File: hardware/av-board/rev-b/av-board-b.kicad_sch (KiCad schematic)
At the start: 163 parts, among them J1 RCA Y, J10 2x20 socket, J2 RCA Pb, J3 RCA Pr, J4 RCA L, J5 RCA R, J6 HDMI-001, J9 2x20 socket, SW1 TS-1187A-B-A-B, SW2 TS-1187A-B-A-B, U1 ADV7181DBCPZ-RL, U10 TPD4E05U06DQAR, U11 TPD4E05U06DQAR, U2 ADV7511KSTZ, U3 PCM1808PWR, U4 TLV62569DBVR, U5 TPS7A7001DDAR, U6 TPS7A7001DDAR, U7 TPS7A7001DDAR, U8 TPD4E05U06DQAR, U9 TPD4E05U06DQAR, Y1 28.63636MHz 20pF

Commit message: AV boards: second full review, ESD at the connectors, rev C, rev B and C-B routed
Rev C (the SOM on its own carrier, C-A with the ADV7511, C-B with the SN65DP159) joins rev B on
shared code: kit/circuits.py (rev B's circuits), kit/adv7181d_layout.py, kit/tmds_layout.py,
rev-c/ (carrier, floor plan, SOM pin matching, design notes, review).

Review fixes (rev-b/review.md, rev-c/review.md):
- ESD at each connector: a TPD1E05U06 per video and S/PDIF input (the shared four-line arrays
  sat 11-25 mm from some of their connectors); every ESD part placed first, at its connector;
  an array's ground through the package to one via away from the connector (TI's layout); the
  VGA array's channels in the header's order; rev C's USB-C TVS between receptacle and fuse.
- XIAO: an ESP32-C3 boots right (SCK pulled up for GPIO8, TMS on D0 for GPIO2, 470 R on the
  translator's outputs for GPIO9's BOOT button).
- Rev B: J10 pins 29/30 (the Console's SDRAM EXIO pins, which a MiSTer-style fit puts on 3.3 V
  and GND) left open.
- D6 drawn as the unidirectional TVS it is.

Kit: plane vias never in pads, by true circle-to-box distance; analog lines and references kept
0.5 mm from digital ones by the router (Freerouting class-to-class rules); rip-up in the
finisher, kept only when it leaves fewer gaps; xtalk.py counts each close run once.

Rev B and C-B: routed, DRC clean, no unconnected items; schematics, fab files and renders
regenerated. C-A's routed board follows.

Co-Authored-By: Claude Opus 5.5 <noreply@anthropic.com>
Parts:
- removed FB5: 120R, Inductor_SMD:L_0603_1608Metric, symbol Device:FerriteBead
- removed U11: TPD4E05U06DQAR, lcsc:USON-10_L2.5-W1.0-P0.50-BL, symbol lcsc:TPD4E05U06DQAR_C138714
- added C77, C81, C82, C83, C84, C85, C86, C87, C88, C89, C90, C91, C92: 100n, Capacitor_SMD:C_0402_1005Metric, symbol Device:C
- added C78, C79, C80: 10u, Capacitor_SMD:C_0603_1608Metric, symbol Device:C
- added D10, D11, D12, D13, D8, D9: TPD1E05U06DPYR, lcsc:X1SON-2_L1.0-W0.6-P0.65-RD-1, symbol lcsc:TPD1E05U06DPYR
- added D2: KT-0603R, lcsc:LED-SMD_L1.6-W0.8-R-RD, symbol lcsc:KT-0603R
- added D3: B5819W, Diode_SMD:D_SOD-123, symbol Device:D_Schottky
- added D7: 1N4148WS, Diode_SMD:D_SOD-323, symbol Device:D
- added F2: 0.2A, lcsc:F0805, symbol lcsc:BSMD0805-020-30V
- added J11: XIAO 5V..D7, lcsc:HDR-TH_7P-P2.54-V-F, symbol lcsc:HXPM2.54-1X7PZC-Y
- added J12: XIAO D0..D6, lcsc:HDR-TH_7P-P2.54-V-F, symbol lcsc:HXPM2.54-1X7PZC-Y
- added J13: SPDIF, lcsc:HDR-TH_5P-P2.54-V-M, symbol lcsc:PZ254V-11-05P
- added J7: SYNC, lcsc:HDR-TH_2P-P2.54-V-M, symbol lcsc:PZ254V-11-02P
- added J8: VGA, lcsc:HDR-TH_16P-P2.54-V-M-R2-C8-S2.54, symbol lcsc:Header-Male-2.54_2x8
- added Q1, Q2: 2N7002, lcsc:SOT-23-3_L2.9-W1.3-P1.90-LS2.4-BR, symbol lcsc:2N7002
- added R52: 47k, Resistor_SMD:R_0402_1005Metric, symbol Device:R
- added R53, R54, R55, R57, R59, R77: 10k, Resistor_SMD:R_0402_1005Metric, symbol Device:R
- added R56, R58: 12k, Resistor_SMD:R_0402_1005Metric, symbol Device:R
- added R60: 75, Resistor_SMD:R_0603_1608Metric, symbol Device:R
- added R61: 1M, Resistor_SMD:R_0402_1005Metric, symbol Device:R
- added R62, R64: 33, Resistor_SMD:R_0402_1005Metric, symbol Device:R
- added R63: 100k, Resistor_SMD:R_0402_1005Metric, symbol Device:R
- added R65, R66, R67, R68, R69: 49.9, Resistor_SMD:R_0402_1005Metric, symbol Device:R
- added R70: 887, Resistor_SMD:R_0402_1005Metric, symbol Device:R
- added R71, R72, R73, R74, R75, R76: 2k, Resistor_SMD:R_0402_1005Metric, symbol Device:R
- added R78: 27k, Resistor_SMD:R_0402_1005Metric, symbol Device:R
- added U12: TPS7A2045PDBVR, lcsc:SOT-23-5_L2.9-W1.6-P0.95-LS2.8-BR, symbol lcsc:TPS7A2045PDBVR
- added U13: SN74LVC1GU04DBVR, lcsc:SOT-23-5_L3.0-W1.7-P0.95-LS2.8-BR, symbol lcsc:SN74LVC1GU04DBVR
- added U14, U15: SN74LVC1G04DBVR, lcsc:SOT-23-5_L3.0-W1.7-P0.95-LS2.8-BR, symbol lcsc:SN74LVC1G04DBVR
- added U19, U20: TPD4E05U06DQAR, lcsc:USON-10_L2.5-W1.0-P0.50-BL, symbol lcsc:TPD4E05U06DQAR_C138714
- added U21: SN74LVC2G17DBVR, lcsc:SOT-23-6_L2.9-W1.6-P0.95-LS2.8-BL, symbol lcsc:SN74LVC2G17DBVR
- added U22: SN74LVC8T245PWR, lcsc:TSSOP-24_L7.8-W4.4-P0.65-LS6.4-BL, symbol lcsc:SN74LVC8T245PWR
- added U23: SN74AVC4T245PWR, lcsc:TSSOP-16_L5.0-W4.4-P0.65-LS6.4-BL, symbol lcsc:SN74AVC4T245PWR
- C11: value 10u -> 6.8p; footprint Capacitor_SMD:C_0805_2012Metric -> Capacitor_SMD:C_0402_1005Metric; LCSC C15850 -> C1576
- C12, C15, C9: value 220p -> 10u; footprint Capacitor_SMD:C_0402_1005Metric -> Capacitor_SMD:C_0805_2012Metric; LCSC C1530 -> C15850
- C14: value 10u -> 220p; footprint Capacitor_SMD:C_0805_2012Metric -> Capacitor_SMD:C_0402_1005Metric; LCSC C15850 -> C1530
- C16, C18, C19: footprint Capacitor_SMD:C_0603_1608Metric -> Capacitor_SMD:C_0805_2012Metric; LCSC C19702 -> C15850
- C17, C20: value 10u -> 220p; footprint Capacitor_SMD:C_0603_1608Metric -> Capacitor_SMD:C_0402_1005Metric; LCSC C19702 -> C1530
- C23, C24, C66, C68: value 100n -> 10u; footprint Capacitor_SMD:C_0402_1005Metric -> Capacitor_SMD:C_0603_1608Metric; LCSC C1525 -> C19702
- C26: value 1n -> 100n; LCSC C1523 -> C1525
- C27: value 33p -> 100n; LCSC C1562 -> C1525
- C28: value 33p -> 1n; LCSC C1562 -> C1523
- C29: value 100n -> 1n; LCSC C1525 -> C1523
- C30: value 100n -> 33p; LCSC C1525 -> C1562
- C31: value 10u -> 33p; footprint Capacitor_SMD:C_0603_1608Metric -> Capacitor_SMD:C_0402_1005Metric; LCSC C19702 -> C1562
- C33, C46, C48, C50, C52, C54: value 10n -> 100n; LCSC C15195 -> C1525
- C34, C37: footprint Capacitor_SMD:C_0603_1608Metric -> Capacitor_SMD:C_0402_1005Metric; LCSC C19702 -> C15525
- C39: value 10u -> 10n; footprint Capacitor_SMD:C_0603_1608Metric -> Capacitor_SMD:C_0402_1005Metric; LCSC C19702 -> C15195
- C40: value 100n -> 10u; LCSC C1525 -> C15525
- C41: value 82n -> 100n; LCSC C277511 -> C1525
- C42: value 10n -> 10u; LCSC C15195 -> C15525
- C44: value 10n -> 82n; LCSC C15195 -> C277511
- C45, C51, C53, C55, C57, C59: value 100n -> 10n; LCSC C1525 -> C15195
- C5, C7, C8: value 10u -> 100n; footprint Capacitor_SMD:C_0805_2012Metric -> Capacitor_SMD:C_0402_1005Metric; LCSC C15850 -> C1525
- C56, C58, C60: value 10u -> 100n; footprint Capacitor_SMD:C_0603_1608Metric -> Capacitor_SMD:C_0402_1005Metric; LCSC C19702 -> C1525
- C6: value 6.8p -> 100n; LCSC C1576 -> C1525
- C61: value 220p -> 10n; LCSC C1530 -> C15195
- C63: value 220p -> 100n; LCSC C1530 -> C1525
- C64: value 1u -> 10u; LCSC C15849 -> C19702
- C69, C71: value 100n -> 220p; LCSC C1525 -> C1530
- C70, C72: value 100n -> 1u; footprint Capacitor_SMD:C_0402_1005Metric -> Capacitor_SMD:C_0603_1608Metric; LCSC C1525 -> C15849
- R10, R8: value 30.1k -> 10k; LCSC C29402 -> C25744
- R11, R12: value 75 -> 10k; footprint Resistor_SMD:R_0603_1608Metric -> Resistor_SMD:R_0402_1005Metric; LCSC C4275 -> C25744
- R13: value 75 -> 499k; footprint Resistor_SMD:R_0603_1608Metric -> Resistor_SMD:R_0402_1005Metric; LCSC C4275 -> C25793
- R14: value 1M -> 100k; LCSC C26083 -> C25741
- R15: value 1.69k -> 169k; LCSC C25870 -> C25758
- R16, R18, R20: value 33 -> 30.1k; LCSC C25105 -> C29402
- R17, R19: value 33 -> 78.7k; LCSC C25105 -> C67239
- R21, R22, R23: value 33 -> 75; footprint Resistor_SMD:R_0402_1005Metric -> Resistor_SMD:R_0603_1608Metric; LCSC C25105 -> C4275
- R24: value 4.7k -> 75; footprint Resistor_SMD:R_0402_1005Metric -> Resistor_SMD:R_0603_1608Metric; LCSC C25900 -> C4275
- R25: value 4.7k -> 1M; LCSC C25900 -> C26083
- R26: value 4.7k -> 1.69k; LCSC C25900 -> C25870; Note held in reset until the FPGA drives it (5 ms low minimum [D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 -> (none)
- R27, R28, R29: value 4.7k -> 33; LCSC C25900 -> C25105
- R3: value 499k -> 470; LCSC C25793 -> C25117
- R30, R31, R32, R33, R34: value 10k -> 33; LCSC C25744 -> C25105
- R35, R36, R38, R39: value 10k -> 4.7k; LCSC C25744 -> C25900
- R37: value 10k -> 4.7k; LCSC C25744 -> C25900; Note (none) -> held in reset until the FPGA drives it (5 ms low minimum [D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
- R40: value 49.9 -> 4.7k; LCSC C25120 -> C25900
- R41: value 49.9 -> 10k; LCSC C25120 -> C25744
- R42, R43: value 49.9 -> 75; footprint Resistor_SMD:R_0402_1005Metric -> Resistor_SMD:R_0603_1608Metric; LCSC C25120 -> C4275
- R44: value 887 -> 75; footprint Resistor_SMD:R_0402_1005Metric -> Resistor_SMD:R_0603_1608Metric; LCSC C55968414 -> C4275
- R45, R46: value 2k -> 10k; LCSC C4109 -> C25744
- R47, R48: value 2k -> 33; LCSC C4109 -> C25105
- R49: value 2k -> 4.7k; LCSC C4109 -> C25900
- R5: value 169k -> 470; LCSC C25758 -> C25117
- R50: value 2k -> 47k; LCSC C4109 -> C25792
- R51: value 10k -> 4.7k; LCSC C25744 -> C25900; Note 0 V on HPD with no sink [HWG 6.1.4: 10 k +-10 %] -> (none)
- R6: value 30.1k -> 470; LCSC C29402 -> C25117
- R7, R9: value 78.7k -> 10k; LCSC C67239 -> C25744
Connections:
- net +5V: now also C62.1, C9.1, D3.2 (A), F2.1, U12.1 (IN), U12.3 (EN); no longer C4.1
- net 1V8A: now also C16.1, C17.1, R17.1; no longer C11.1, C12.1, R7.1
- net 1V8B: now also C19.1, C20.1, R19.1; no longer C14.1, C15.1, R9.1
- net 3V3: now also C14.1, C15.1, C18.1, C49.1, C6.1, C67.1, C68.1, C76.1, R10.2, R11.2, R12.2, R15.1, R35.1, R36.1, R49.1, R51.1, C77.1, C91.1, Q1.1 (G), Q2.1 (G), R71.1, R72.1, R73.1, R78.1, U13.5 (VCC), U14.5 (VCC), U15.5 (VCC), U21.5 (VCC), U22.23 (VCCB), U22.24 (VCCB), U23.16 (VCCB); no longer C10.1, C59.1, C60.1, C9.1, R24.1, R25.1, R45.1, R46.1, R47.1, R5.1
- net 3V6: now also C10.1, C11.1, C12.1, R13.1; no longer C5.1, C6.1, C7.1, R3.1
- net 5VA: now also C65.1, C66.1, U12.5 (OUT); no longer C57.1, C58.1
- net AIN_PB: now also C26.2; no longer C24.2
- net AIN_PR: now also C27.2; no longer C25.2
- net AIN_Y: now also C25.2; no longer C23.2
- net ALSB: now also R39.2; no longer R28.2
- net AUD_DIV_L: now also C69.1, C70.1, R56.2, R57.1; no longer C61.1, C62.1, R36.2, R37.1
- net AUD_DIV_R: now also C71.1, C72.1, R58.2, R59.1; no longer C63.1, C64.1, R38.2, R39.1
- net AUD_VINL: now also C70.2; no longer C62.2
- net AUD_VINR: now also C72.2; no longer C64.2
- net AV_AVDD: now also C23.1, C60.1, C61.1; no longer C18.1, C53.1, C54.1
- net AV_C0: now also R31.1; no longer R20.1
- net AV_C1: now also R30.1; no longer R19.1
- net AV_C5: now also R29.1; no longer R18.1
- net AV_C6: now also R28.1; no longer R17.1
- net AV_C7: now also R27.1; no longer R16.1
- net AV_DE: now also R34.1; no longer R23.1
- net AV_DVDD: now also C21.1, C54.1, C55.1, C56.1, C57.1; no longer C16.1, C47.1, C48.1, C49.1, C50.1
- net AV_DVDDIO: now also C24.1, C50.1, C51.1, C52.1, C53.1, R38.1, R39.1, R40.1; no longer C19.1, C43.1, C44.1, C45.1, C46.1, R27.1, R28.1, R29.1
- net AV_HS: now also R32.1; no longer R21.1
- net AV_PVDD: now also C22.1, C44.2, C45.2, C58.1, C59.1; no longer C17.1, C41.2, C42.2, C51.1, C52.1
- net AV_VS: now also R33.1; no longer R22.1
- net CAPC2: now also C37.1, C38.1, C39.1; no longer C34.1, C35.1, C36.1
- net CAPY1: now also C34.1, C35.1, C36.1; no longer C31.1, C32.1, C33.1
- net CAPY2: now also C32.1, C33.1, C37.2, C38.2, C39.2; no longer C29.1, C30.1, C31.2, C32.2, C33.2
- net CML: now also C42.1, C43.1; no longer C39.1, C40.1
- net ELPF: now also C45.1, R26.1; no longer C42.1, R15.1
- net ELPF_RC: now also C44.1, R26.2; no longer C41.1, R15.2
- net FB_1V8A: now also C17.2, R17.2, R18.1; no longer C12.2, R7.2, R8.1
- net FB_1V8B: now also C20.2, R19.2, R20.1; no longer C15.2, R10.1, R9.2
- net FB_3V3: now also C14.2, R15.2, R16.1; no longer C9.2, R5.2, R6.1
- net FB_3V6: now also C11.2, R13.2, R14.1; no longer C6.2, R3.2, R4.1
- net FMT: now also R55.1; no longer R35.1
- net GND: now also C12.2, C15.2, C23.2, C24.2, C31.2, C32.2, C33.2, C41.2, C42.2, C6.2, C62.2, C64.2, C9.2, R14.2, R16.2, R18.2, R20.2, R21.2, R22.2, R23.2, R24.2, R41.2, R42.2, R43.2, R45.2, R46.2, R9.2, C77.2, C78.2, C79.2, C80.2, C81.2, C82.2, C83.2, C84.2, C85.2, C86.2, C87.2, C88.2, C89.2, C90.2, C91.2, C92.2, D10.2 (GND), D11.2 (GND), D12.2 (GND), D13.2 (GND), D2.2 (K), D8.2 (GND), D9.2 (GND), J11.2, J13.2, J13.4, J7.2, J8.10, J8.5, J8.6, J8.7, J8.8, R53.2, R54.2, R55.2, R57.2, R59.2, R60.2, R63.2, R70.2, R74.2, R77.2, U12.2 (GND), U13.3 (GND), U14.3 (GND), U15.3 (GND), U19.3 (GND), U19.8 (GND), U20.3 (GND), U20.8 (GND), U21.2 (GND), U22.10 (A8), U22.11 (GND), U22.12 (GND), U22.13 (GND), U22.22 (~{OE}), U22.6 (A4), U22.7 (A5), U22.8 (A6), U22.9 (A7), U23.10 (2B2), U23.11 (2B1), U23.14 (2#OE), U23.15 (1#OE), U23.2 (1DIR), U23.3 (2DIR), U23.8 (GND), U23.9 (GND); no longer C11.2, C14.2, C17.2, C20.2, C27.2, C28.2, C29.2, C37.2, C38.2, C39.2, C44.2, C45.2, C46.2, C47.2, C48.2, C70.2, C72.2, C74.2, J10.27, J10.28, J10.29, J10.30, J10.33, J10.34, J10.35, J10.36, J9.31, J9.32, J9.33, J9.34, J9.35, J9.36, R10.2, R11.2, R12.2, R13.2, R26.2, R30.2, R31.2, R32.2, R33.2, R34.2, R35.2, R39.2, R48.2, R51.2, R6.2, R8.2, U2.10 (SPDIF), U2.48 (CEC), U2.50 (CEC_CLK)
- net HDMI_5V: now also C92.1, F2.2, R75.1, R76.1; no longer C76.1, F1.2, R49.1, R50.1, U8.5 (D2-), U8.6 (NC)
- net HDMI_HPD: now also R77.1; no longer R51.1
- net HDMI_SCL: now also R75.2; no longer R49.2
- net HDMI_SDA: now also R76.2; no longer R50.2
- net IN_C0: now also R31.2; no longer R20.2
- net IN_C1: now also R30.2; no longer R19.2
- net IN_C5: now also R29.2; no longer R18.2
- net IN_C6: now also R28.2; no longer R17.2
- net IN_C7: now also R27.2; no longer R16.2
- net IN_DE: now also R34.2; no longer R23.2
- net IN_HS: now also R32.2; no longer R21.2
- net IN_INT: now also R38.2; no longer R27.2
- net IN_RESET_N: now also R37.1; no longer R26.1
- net IN_SCL: now also R35.2; no longer R24.2
- net IN_SDA: now also R36.2; no longer R25.2
- net IN_VS: now also R33.2; no longer R22.2
- net MD0: now also R53.1; no longer R33.1
- net MD1: now also R54.1; no longer R34.1
- net OUT_I2S0: now also R68.1; no longer R43.1
- net OUT_INT: now also R73.2; no longer R47.2
- net OUT_LRCLK: now also R67.1; no longer R42.1
- net OUT_MCLK: now also R65.1; no longer R40.1
- net OUT_PD: now also R74.1; no longer R48.1
- net OUT_SCL: now also R71.2; no longer R45.2
- net OUT_SCLK: now also R66.1; no longer R41.1
- net OUT_SDA: now also R72.2; no longer R46.2
- net PD_FB: now also R41.1; no longer R30.1
- net PWRDWN: now also R40.2; no longer R29.2
- net RCA_L: now also R56.1; no longer R36.1
- net RCA_PB: now also C26.1, R22.1, D9.1 (I/O); no longer C24.1, R12.1
- net RCA_PR: now also C27.1, R23.1, D10.1 (I/O); no longer C25.1, R13.1
- net RCA_R: now also R58.1; no longer R38.1
- net RCA_Y: now also C25.1, C28.1, R21.1, D8.1 (I/O); no longer C23.1, C26.1, R11.1
- net REFOUT: now also C40.1, C41.1; no longer C37.1, C38.1
- net R_EXT: now also R70.1; no longer R44.1
- net SYNC_Y: now also C28.2; no longer C26.2
- net TX_AVDD: now also C79.1, C85.1, C86.1, C87.1, C88.1; no longer C21.1, C69.1, C70.1, C71.1, C72.1
- net TX_DVDD: now also C78.1, C81.1, C82.1, C83.1, C84.1; no longer C20.1, C65.1, C66.1, C67.1, C68.1
- net TX_I2S0: now also R68.2; no longer R43.2
- net TX_LRCLK: now also R67.2; no longer R42.2
- net TX_MCLK: now also R65.2; no longer R40.2
- net TX_PLVDD: now also C80.1, C89.1, C90.1; no longer C22.1, C73.1, C74.1
- net TX_SCLK: now also R66.2; no longer R41.2
- net VREF: now also C63.1, C64.1; no longer C55.1, C56.1
- net XTAL: now also C30.1, R25.1; no longer C27.1, R14.1
- net XTAL1: now also C31.1, R25.2; no longer C28.1, R14.2
- net SYNC_G: now reaches U1.33 (SOG)
- net SYNC_G: now also C29.2
- net AIN_VG: now reaches U1.35 (AIN2)
- net AIN_VG: now also C47.2
- net AIN_VR: now reaches U1.46 (AIN7)
- net AIN_VR: now also C46.2
- net AIN_VB: now reaches U1.48 (AIN9)
- net AIN_VB: now also C48.2
- net HDMI_CEC: now reaches J6.13 (CEC)
- net HDMI_CEC: now also U2.48 (CEC), U8.5 (D2-), U8.6 (NC), D7.1 (K)
- net PD_HS_IN_CS_IN renamed VGA_HSIN
- net VGA_HSIN: now also R47.2; no longer R31.1
- net PD_VS_IN renamed VGA_VSIN
- net VGA_VSIN: now also R48.2; no longer R32.1
- new net CEC_PU: D7.2 (A), R78.2
- new net ESP_CS: J9.32, R10.1, U22.21 (B1)
- new net ESP_IRQ: J9.33, R11.1, U23.13 (1B1)
- new net ESP_MISO: J9.35, R12.1, U23.12 (1B2)
- new net ESP_MOSI: J9.36, U22.19 (B3)
- new net ESP_SCK: J9.34, U22.20 (B2)
- new net IN_LED: J10.33, R3.1
- new net LED_A: D2.1 (A), R3.2
- new net OUT_CECCLK: J9.31, U2.50 (CEC_CLK)
- new net OUT_SPDIF: J10.28, R69.1
- new net RCA_SYNC: C29.1, D11.1 (I/O), J7.1, R24.1
- new net SPDIF_5V: C73.1, F1.2, J13.5
- new net SPDIF_AC: C74.2, R61.2, U13.2 (A)
- new net SPDIF_AMP: R61.1, U13.4 (Y), U14.2 (A)
- new net SPDIF_COAX: C74.1, D12.1 (I/O), J13.1, R60.1
- new net SPDIF_OPT: D13.1 (I/O), J13.3, R63.1, U15.2 (A)
- new net SPDIF_ORX: J10.35, R64.2
- new net SPDIF_OSQ: R64.1, U15.4 (Y)
- new net SPDIF_RX: J10.27, R62.2
- new net SPDIF_SQ: R62.1, U14.4 (Y)
- new net TX_SPDIF: R69.2, U2.10 (SPDIF)
- new net VGA_5V: J8.9, R50.1, R52.1
- new net VGA_B: C48.1, J8.3, R44.1, U19.5 (D2-), U19.6 (NC)
- new net VGA_G: C47.1, J8.2, R43.1, U19.2 (D1-), U19.9 (NC)
- new net VGA_HS: J8.13, R45.1, U20.1 (D1+), U20.10 (NC), U21.1 (1A)
- new net VGA_HSB: R47.1, U21.6 (1Y)
- new net VGA_R: C46.1, J8.1, R42.1, U19.4 (D2+), U19.7 (NC)
- new net VGA_SCL: J8.15, Q2.3 (D), R52.2, U20.5 (D2-), U20.6 (NC)
- new net VGA_SCL_F: J10.34, Q2.2 (S), R51.2
- new net VGA_SDA: J8.12, Q1.3 (D), R50.2, U20.4 (D2+), U20.7 (NC)
- new net VGA_SDA_F: J10.36, Q1.2 (S), R49.2
- new net VGA_VS: J8.14, R46.1, U20.2 (D1-), U20.9 (NC), U21.3 (2A)
- new net VGA_VSB: R48.1, U21.4 (2Y)
- new net XIAO_3V3: C5.1, C7.1, J11.3, R4.1, R7.2, R8.2, U22.1 (VCCA), U22.2 (DIR), U23.1 (VCCA)
- new net XIAO_5V: C4.1, D3.1 (K), J11.1
- new net XIAO_D10: J11.4, R9.1, U22.5 (A3)
- new net XIAO_D4: J12.5, R7.1, U22.3 (A1)
- new net XIAO_D5: J12.6, R5.2
- new net XIAO_D5_A: R5.1, U23.4 (1A1)
- new net XIAO_D8: J11.6, R8.1, U22.4 (A2)
- new net XIAO_D9: J11.5, R6.2
- new net XIAO_D9_A: R6.1, U23.5 (1A2)
- no-connect marks 22 -> 39
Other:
- moved on the sheet: C1, C10, C11, C12, C13, C14, C15, C16, C17, C18, C19, C2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

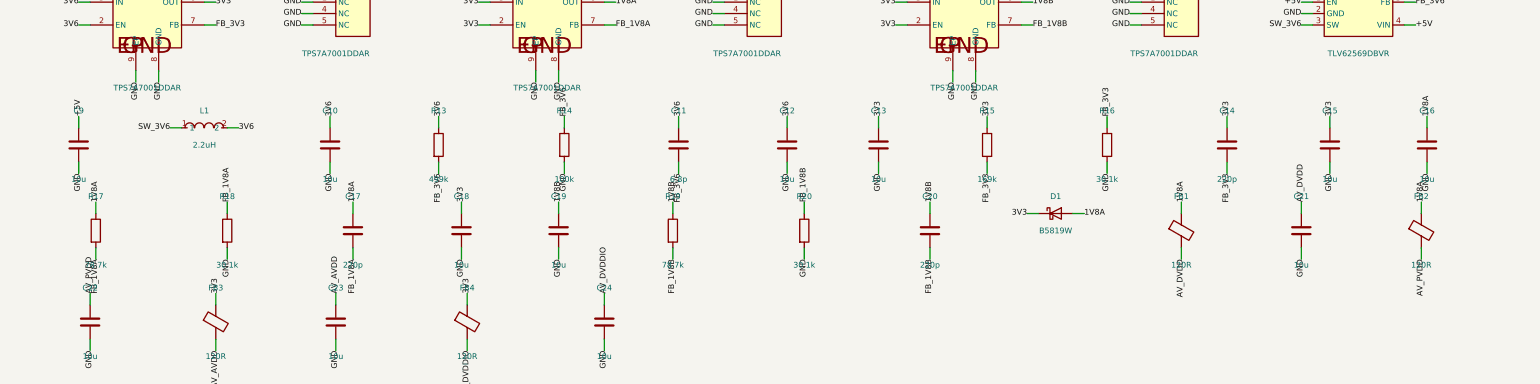
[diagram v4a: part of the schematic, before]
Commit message: AV boards: rev B, C-B routed on the fixed placement; prune side-by-side copies; JLC jack rotation
Every revision: schematic = board.py, the board = its schematic part for part,
ERC and DRC clean, no unconnected items; rev B's, C-A's and C-B's review tables
measured on these routes.

- Rev B: routed on the capacitor placement fixes (try-b-r1, its last gap
  finished); schematic regenerated (eight capacitors renumbered).
- C-B: the 1V1 buck's inductor and output capacitor placed before its feedback
  divider: in the 3V6 bucks' order the divider's 6.8 pF took the inductor's place
  beside SW, the inductor went above the chip with its SW pad turned away (10.7 mm
  of SW track, FB's copper 0.2 mm from it). Routed again (try-cb-q3): SW 4.1 mm,
  FB 3.0 mm from it; nothing digital within 0.5 mm of an analog line but XTAL1
  beside LLC at the pins' pitch.
- C-A: its review column measured on the route; CPL jack rotations.
- kit/pcbkit.py prune: copper laid side by side taken up too (beside(): the
  shorter of each kit/doubled.py pair), every candidate checked by DRC on a copy
  of the file's text first (save_without(), removable()), so nothing taken out of
  a pcbnew board is put back; rounds run with faulthandler and report a crash's
  signal (one round had segfaulted in libstdc++ with no message).
- kit/pcbkit.py finish_unconnected: a gap's three nearest pad pairs tried in turn
  (rev B's TX_PLVDD pin 21 was walled in towards pin 26, not towards its own
  capacitor).
- kit/gen_fab.py JLC_TURN: JLCPCB places a part by its own footprint for the LCSC
  number; for RCJ-014 and RCJ-017 that is ours turned 90 degrees, so the CPL
  turns those jacks back (their preview had the barrels along the board edge).
  RCJ-012 has no footprint there and is placed as drawn.

Co-Authored-By: Claude Opus 5.5 <noreply@anthropic.com>
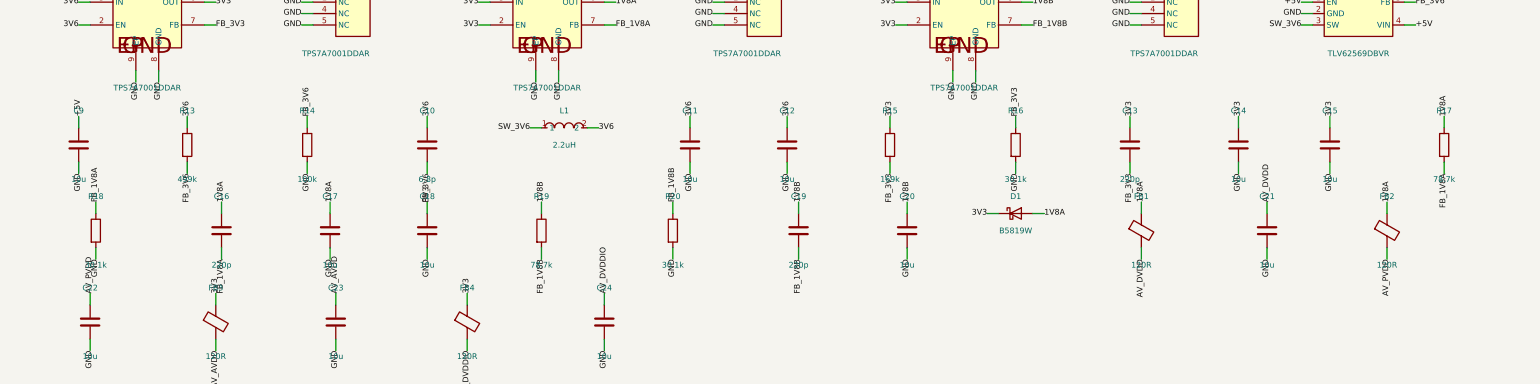
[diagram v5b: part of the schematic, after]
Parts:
- C10: value 10u -> 6.8p; footprint Capacitor_SMD:C_0805_2012Metric -> Capacitor_SMD:C_0402_1005Metric; LCSC C15850 -> C1576
- C11: value 6.8p -> 10u; footprint Capacitor_SMD:C_0402_1005Metric -> Capacitor_SMD:C_0805_2012Metric; LCSC C1576 -> C15850
- C13, C16, C19: value 10u -> 220p; footprint Capacitor_SMD:C_0805_2012Metric -> Capacitor_SMD:C_0402_1005Metric; LCSC C15850 -> C1530
- C14, C17, C20: value 220p -> 10u; footprint Capacitor_SMD:C_0402_1005Metric -> Capacitor_SMD:C_0805_2012Metric; LCSC C1530 -> C15850
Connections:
- net FB_1V8A: now also C16.2; no longer C17.2
- net FB_1V8B: now also C19.2; no longer C20.2
- net FB_3V3: now also C13.2; no longer C14.2
- net FB_3V6: now also C10.2; no longer C11.2
- net GND: now also C11.2, C14.2, C17.2, C20.2; no longer C10.2, C13.2, C16.2, C19.2
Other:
- moved on the sheet: C10, C11, C13, C14, C16, C17, C18, C19, C20, C21, D1, FB1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
